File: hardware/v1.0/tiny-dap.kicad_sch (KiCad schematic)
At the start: 22 parts, among them J1 Conn_02x04_Odd_Even, J2 USB_C_Receptacle_USB2.0, U1 MCU, U2 XC6206PxxxMR

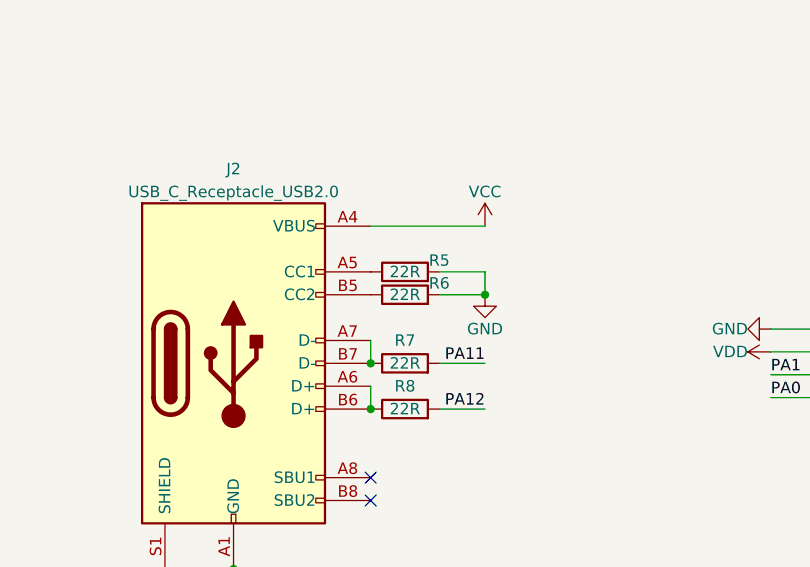
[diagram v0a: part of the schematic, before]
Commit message: hardware bugfix.
- modify usb cc pin res val 22R -> 5K1.

Signed-off-by: UnsicentificLaLaLaLa <zhaohao1997@foxmail.com>
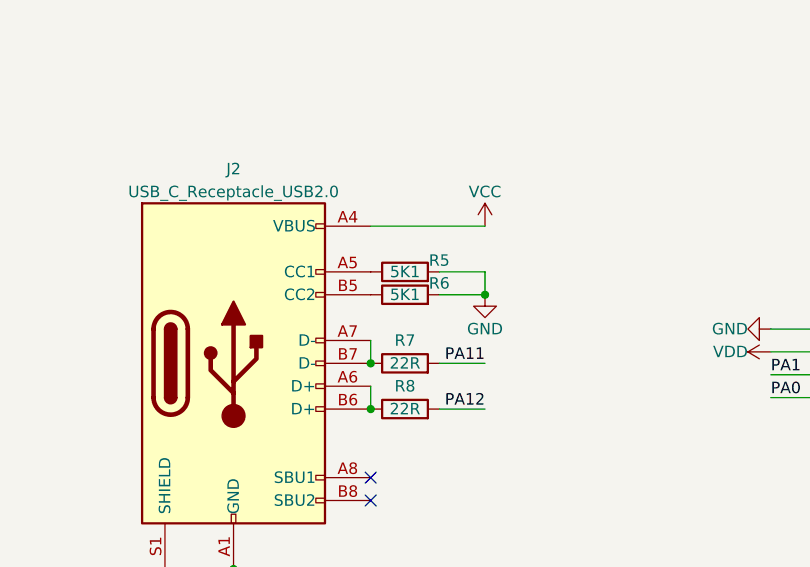
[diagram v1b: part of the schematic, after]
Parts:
- R5, R6: value 22R -> 5K1
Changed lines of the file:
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@@
       (effects (font (size 1.27 1.27)))
     )
-    (property "Value" "22R" (at 137.16 100.33 90)
+    (property "Value" "5K1" (at 137.16 100.33 90)
       (effects (font (size 1.27 1.27)))
     )
@@
       (effects (font (size 1.27 1.27)))
     )
-    (property "Value" "22R" (at 137.16 97.79 90)
+    (property "Value" "5K1" (at 137.16 97.79 90)
       (effects (font (size 1.27 1.27)))
     )
